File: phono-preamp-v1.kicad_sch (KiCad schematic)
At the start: 44 parts, among them J1 Screw_Terminal_01x02, J2 Screw_Terminal_01x02, U1 NE5534, U2 NE5534

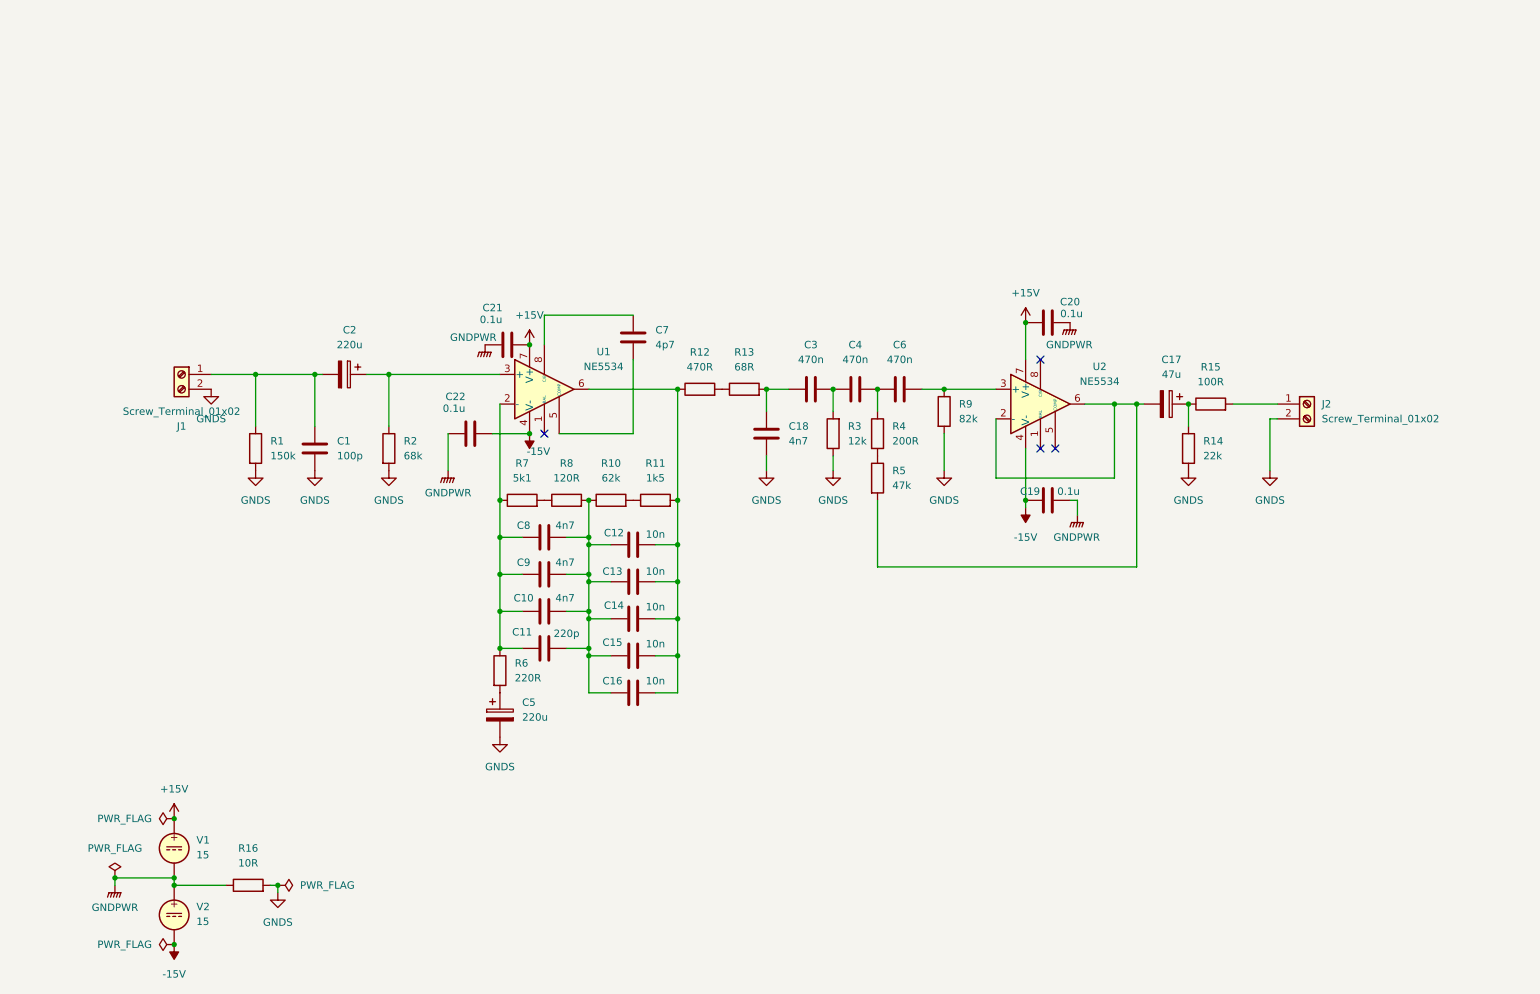
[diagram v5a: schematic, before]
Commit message: Add power input; reannotate
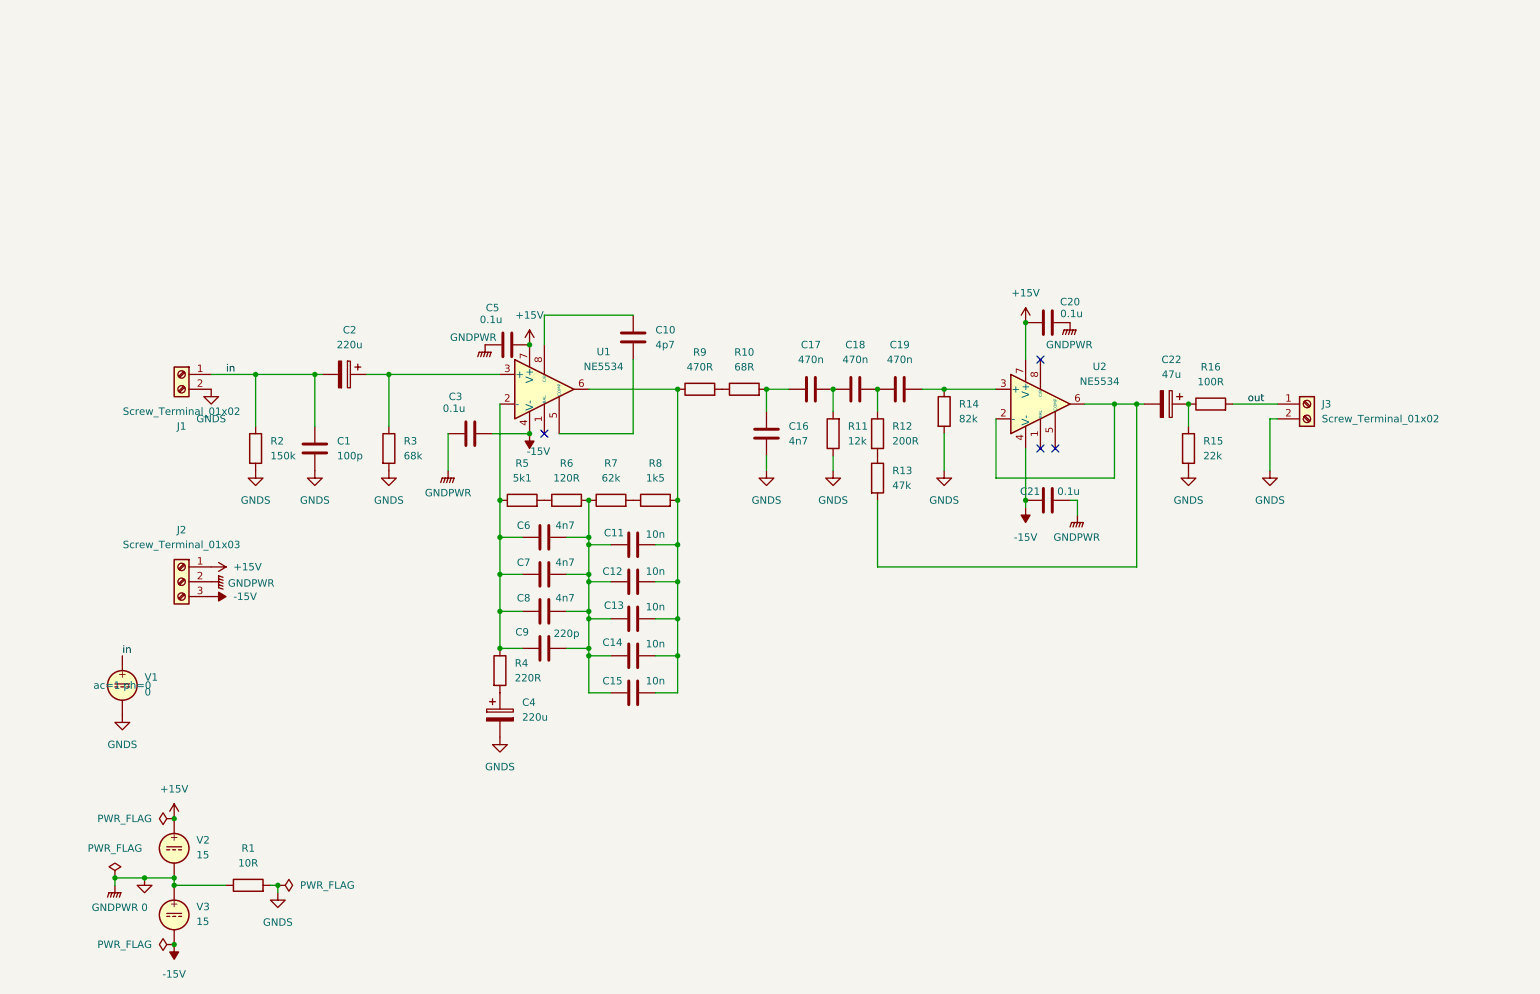
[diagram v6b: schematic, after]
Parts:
- added J2: Screw_Terminal_01x03, TerminalBlock:TerminalBlock_bornier-3_P5.08mm, symbol Connector:Screw_Terminal_01x03
- added V1: 0, symbol Simulation_SPICE:VDC
- C20: footprint (none) -> Capacitor_SMD:C_0805_2012Metric_Pad1.18x1.45mm_HandSolder
- C21: renamed from C19; footprint (none) -> Capacitor_SMD:C_0805_2012Metric_Pad1.18x1.45mm_HandSolder
- C3: renamed from C22; footprint (none) -> Capacitor_SMD:C_0805_2012Metric_Pad1.18x1.45mm_HandSolder
- C5: renamed from C21; footprint (none) -> Capacitor_SMD:C_0805_2012Metric_Pad1.18x1.45mm_HandSolder
- J1: footprint TerminalBlock_4Ucon:TerminalBlock_4Ucon_1x02_P3.50mm_Horizontal -> TerminalBlock:TerminalBlock_bornier-2_P5.08mm
- J3: renamed from J2; footprint TerminalBlock_4Ucon:TerminalBlock_4Ucon_1x02_P3.50mm_Horizontal -> TerminalBlock:TerminalBlock_bornier-2_P5.08mm
- R1: renamed from R16; footprint (none) -> Resistor_SMD:R_0805_2012Metric_Pad1.20x1.40mm_HandSolder
- renumbered C7 to C10, C12 to C11, C13 to C12, C14 to C13, C15 to C14, C16 to C15, C18 to C16, C3 to C17, C4 to C18, C6 to C19, C17 to C22, C5 to C4, C8 to C6, C9 to C7, C10 to C8, C11 to C9, R13 to R10, R3 to R11, R4 to R12, R5 to R13, R9 to R14, R14 to R15, R15 to R16, R1 to R2, R2 to R3, R6 to R4, R7 to R5, R8 to R6, R10 to R7, R11 to R8, R12 to R9, V1 to V2, V2 to V3
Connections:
- net +15V: now also J2.1 (Pin_1)
- net -15V: now also J2.3 (Pin_3)
- net GNDS: now also V1.2
- net in: now reaches C1.1, C2.2, J1.1 (Pin_1), R2.1
- net in: now also V1.1
- net out: now reaches J3.1 (Pin_1), R16.2
- net GNDPWR renamed 0
- net 0: now also J2.2 (Pin_2)
